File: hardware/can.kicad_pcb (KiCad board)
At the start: 2 copper layers, 45 x 35 mm, 42 parts, among them K1 CONN_3, P1 CON-SENSOR, P2 Debug, P3 Boot, SW1 Termination, U1 XMC1XXX48, U2 MCP2562, U3 DRILL, U4 DRILL, U5 DRILL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

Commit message: change text orientation
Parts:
- moved G*** 4.74 mm to (141.3, 89.4), turned to 0 degrees
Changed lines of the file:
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@@
     (links 77)
     (no_connects 0)
-    (area 125.109499 82.909499 170.490501 118.290501)
+    (area 124.445139 82.245139 282.795857 162.890793)
     (thickness 1.6002)
     (drawings 16)
@@
   )
   (setup
-    (last_trace_width 0.2)
+    (last_trace_width 0.249)
     (user_trace_width 0.2)
     (user_trace_width 0.25)
@@
   )
   (module kicad-libraries:Logo_31x31 (layer Vorderseite)
-    (at 144.6 92.8 180)
-    (fp_text reference G*** (at 1.34874 2.97434 180) (layer F.SilkS) hide
+    (at 141.3 89.4)
+    (fp_text reference G*** (at 1.34874 2.97434) (layer F.SilkS) hide
       (effects (font (size 0.29972 0.29972) (thickness 0.0762)))
     )
-    (fp_text value Logo_31x31 (at 1.651 0.59944 180) (layer F.SilkS) hide
+    (fp_text value Logo_31x31 (at 1.651 0.59944) (layer F.SilkS) hide
       (effects (font (size 0.29972 0.29972) (thickness 0.0762)))
     )
@@
     (effects (font (size 0.8001 0.8001) (thickness 0.14986)))
   )
-  (gr_text "Termination\noff - on" (at 155.8 84.7 180) (layer F.SilkS)
+  (gr_text "Termination\noff - on" (at 155.8 84.7) (layer F.SilkS)
     (effects (font (size 0.8 0.8) (thickness 0.15)))
   )
@@
     (effects (font (size 0.8001 0.8001) (thickness 0.200025) italic))
   )
-  (gr_text tinkerforge.com (at 143 88.8 180) (layer F.SilkS)
+  (gr_text tinkerforge.com (at 142.9 93.4) (layer F.SilkS)
     (effects (font (size 0.8001 0.8001) (thickness 0.14986)))
   )
-  (gr_text "CAN\n2.0" (at 128.7 109.6 180) (layer F.SilkS)
+  (gr_text "CAN\n2.0" (at 128.7 109.6) (layer F.SilkS)
     (effects (font (size 0.8001 0.8001) (thickness 0.14986)))
   )

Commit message: fix led text
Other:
- board text added: "Com"
- board text added: "Error"
- board text added: "Status"
- board text removed: "com"
- board text removed: "error"
- board text removed: "status"
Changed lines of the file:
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@@
       (xy 1.301301 2.715081) (xy 1.302426 2.714986)) (layer B.SilkS) (width 0.01))
   )
-  (gr_text error (at 158.8 117) (layer F.SilkS)
+  (gr_text Error (at 158.8 117) (layer F.SilkS)
     (effects (font (size 0.8001 0.8001) (thickness 0.14986)))
   )
-  (gr_text com (at 154.8 117) (layer F.SilkS)
+  (gr_text Com (at 154.8 117) (layer F.SilkS)
     (effects (font (size 0.8001 0.8001) (thickness 0.14986)))
   )
-  (gr_text status (at 150.8 117) (layer F.SilkS)
+  (gr_text Status (at 150.8 117) (layer F.SilkS)
     (effects (font (size 0.8001 0.8001) (thickness 0.14986)))
   )

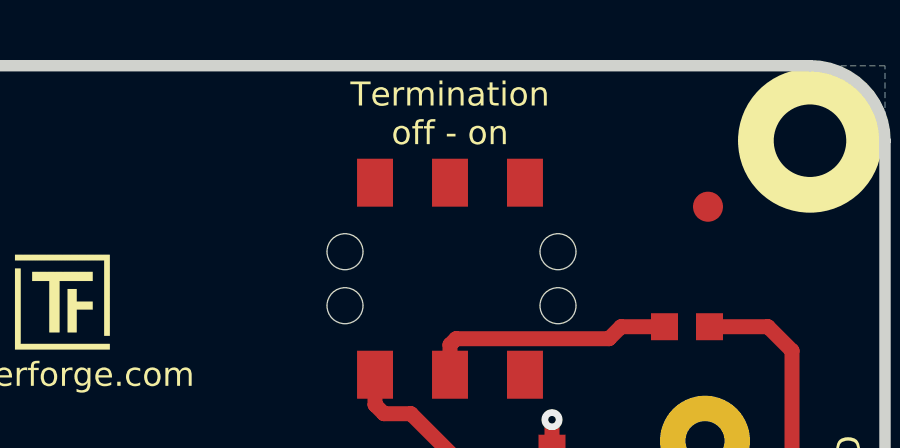
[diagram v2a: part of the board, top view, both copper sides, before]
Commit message: fix text, change logo orientation
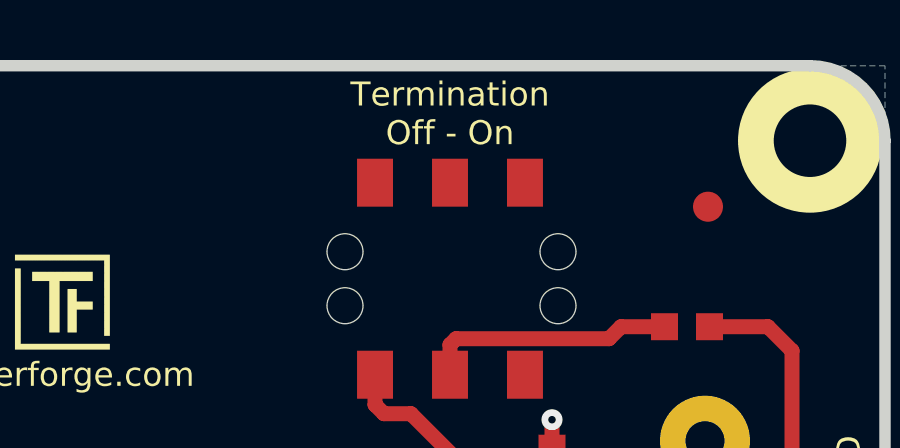
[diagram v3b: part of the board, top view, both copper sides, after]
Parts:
- moved VAL 8.00 mm to (147.8, 100.6)
- moved VAL 8.00 mm to (139.8, 100.6), turned to 180 degrees
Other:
- board text added: "Termination Off - On"
- board text removed: "Termination off - on"
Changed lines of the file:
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@@
     (aux_axis_origin 125.3 118.1)
     (grid_origin 125.3 118.1)
-    (visible_elements FFFF7FBF)
+    (visible_elements FFFFFFBF)
     (pcbplotparams
       (layerselection 0x00030_80000001)
@@
   )
   (module kicad-libraries:WEEE_7mm (layer Rückseite)
-    (at 139.8 100.6 180)
+    (at 147.8 100.6 180)
     (fp_text reference VAL (at 0 0 180) (layer B.SilkS) hide
       (effects (font (size 0.2 0.2) (thickness 0.05)) (justify mirror))
@@
   )
   (module kicad-libraries:CE_5mm (layer Rückseite)
-    (at 147.8 100.6)
-    (fp_text reference VAL (at 0 0) (layer B.SilkS) hide
+    (at 139.8 100.6 180)
+    (fp_text reference VAL (at 0 0 180) (layer B.SilkS) hide
       (effects (font (size 0.2 0.2) (thickness 0.05)) (justify mirror))
     )
-    (fp_text value CE_5mm (at 0 0) (layer B.SilkS) hide
+    (fp_text value CE_5mm (at 0 0 180) (layer B.SilkS) hide
       (effects (font (size 0.2 0.2) (thickness 0.05)) (justify mirror))
     )
@@
     (effects (font (size 0.8001 0.8001) (thickness 0.14986)))
   )
-  (gr_text "Termination\noff - on" (at 155.8 84.7) (layer F.SilkS)
+  (gr_text "Termination\nOff - On" (at 155.8 84.7) (layer F.SilkS)
     (effects (font (size 0.8 0.8) (thickness 0.15)))
   )

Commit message: specify processor
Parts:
- U1: value XMC1XXX48 -> XMC1404
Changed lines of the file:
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@@
   (module kicad-libraries:QFN48-EP2 (layer Vorderseite)
     (at 138.75 110.5 270)
-    (fp_text reference U1 (at 0 0 270) (layer F.SilkS)
-      (effects (font (size 0.29972 0.29972) (thickness 0.0762)))
+    (fp_text reference U1 (at 0 0 270) (layer F.Fab)
+      (effects (font (size 0.29972 0.29972) (thickness 0.07493)))
     )
-    (fp_text value XMC1XXX48 (at 0 -0.7 270) (layer F.SilkS)
-      (effects (font (size 0.29972 0.29972) (thickness 0.0762)))
+    (fp_text value XMC1404 (at 0 -0.7 270) (layer F.Fab)
+      (effects (font (size 0.29972 0.29972) (thickness 0.07493)))
     )
     (fp_circle (center -2.5 2.6) (end -2.4 2.8) (layer F.Fab) (width 0.05))
